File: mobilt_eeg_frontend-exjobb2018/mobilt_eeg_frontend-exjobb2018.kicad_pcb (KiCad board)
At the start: 2 copper layers, 95 x 90.5 mm, 126 parts, among them J1 Conn_02x04_Odd_Even, J11 Conn_01x02, J2 Conn_02x20_Odd_Even, J3 Conn_02x04_Odd_Even, J5 Data Header, J8 Conn_01x08, J9 Conn_01x04, P1 Conn_02x20_Odd_Even, SW1 SW_DIP_x01, SW2 SW_DIP_x01, U1 ADS1299-4PAG, U2 TPS60403DBVR, U3 TPS72325DBVT, U4 TPS73225DBVT, U5 TPS73233DBVT, U6 CAT24C256, U7 arduino_pro_mini_3V3_sparkfun, X1 X1G0044810050_SG7050CAN_2.048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

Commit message: savea for faen
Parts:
- moved J3 51.4 mm to (184.2, 229.6)
- moved J2 50.8 mm to (198.2, 229.6)
- moved R14 49.7 mm to (226.2, 218.2)
- moved R15 49.7 mm to (228.7, 218.2)
- moved R16 49.7 mm to (231.2, 218.2)
- moved R17 49.7 mm to (233.8, 218.2)
- moved R19 49.7 mm to (238.8, 218.2)
- moved R20 49.7 mm to (241.4, 218.2)
- moved R3 49.7 mm to (198.2, 218.2)
- moved R4 49.7 mm to (200.8, 218.2)
- moved R5 49.7 mm to (203.3, 218.2)
- moved R6 49.7 mm to (205.8, 218.2)
- moved R8 49.7 mm to (210.9, 218.2)
- moved R10 49.6 mm to (216.0, 218.2)
- moved R11 49.6 mm to (218.5, 218.2)
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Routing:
- net AGND: track 213.1 -> 156.2 mm, vias 25 -> 5
- net /SRB1: track 32.9 -> 0.00 mm
- net /SRB2: track 32.3 -> 0.00 mm
- net /IN8P: track 31.8 -> 0.00 mm
- net /IN7P: track 29.8 -> 0.00 mm
- net /IN8N: track 29.6 -> 0.00 mm
- net /IN1P: track 28.2 -> 0.00 mm
- net /IN7N: track 28.0 -> 0.00 mm
- net /IN6P: track 27.9 -> 0.00 mm
- net /IN2P: track 27.7 -> 0.00 mm
- net /IN5P: track 26.3 -> 0.00 mm
- net /IN3P: track 26.1 -> 0.00 mm
- net AVSS: track 145.2 -> 119.9 mm
- net /IN4P: track 25.3 -> 0.00 mm
- net /IN6N: track 25.2 -> 0.00 mm
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
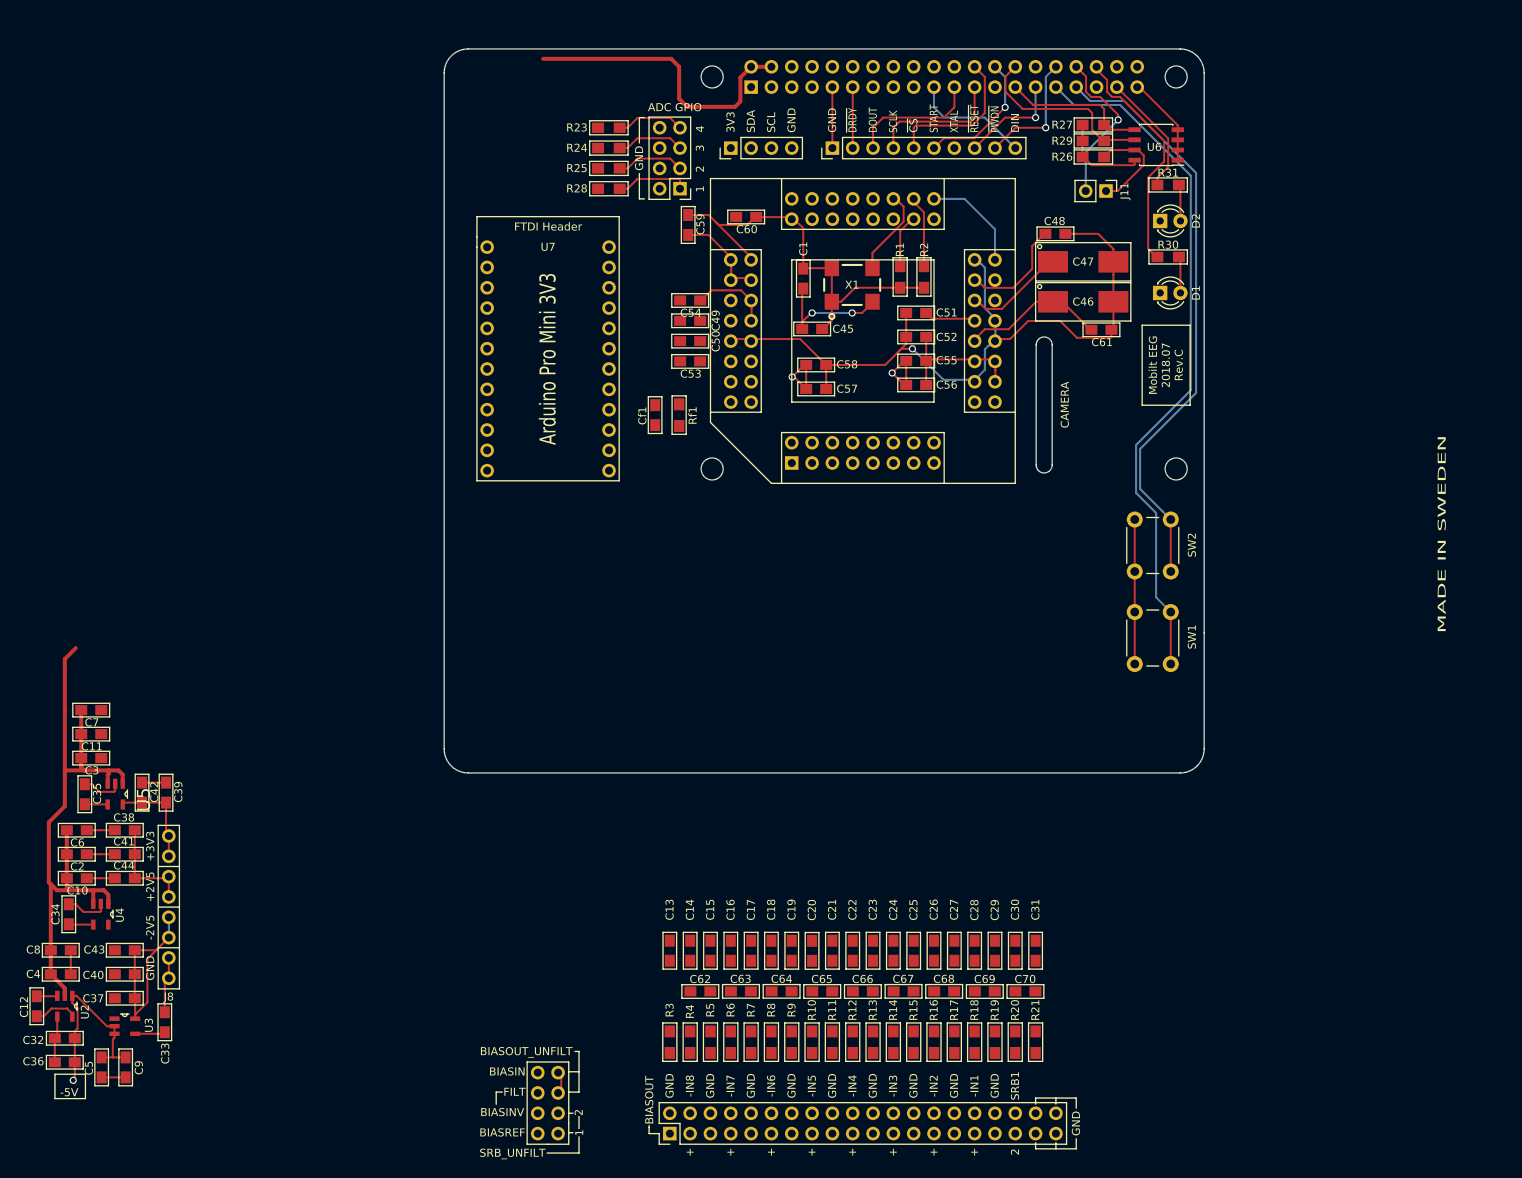
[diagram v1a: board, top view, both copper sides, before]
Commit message: Aligned most stuff except power supply.
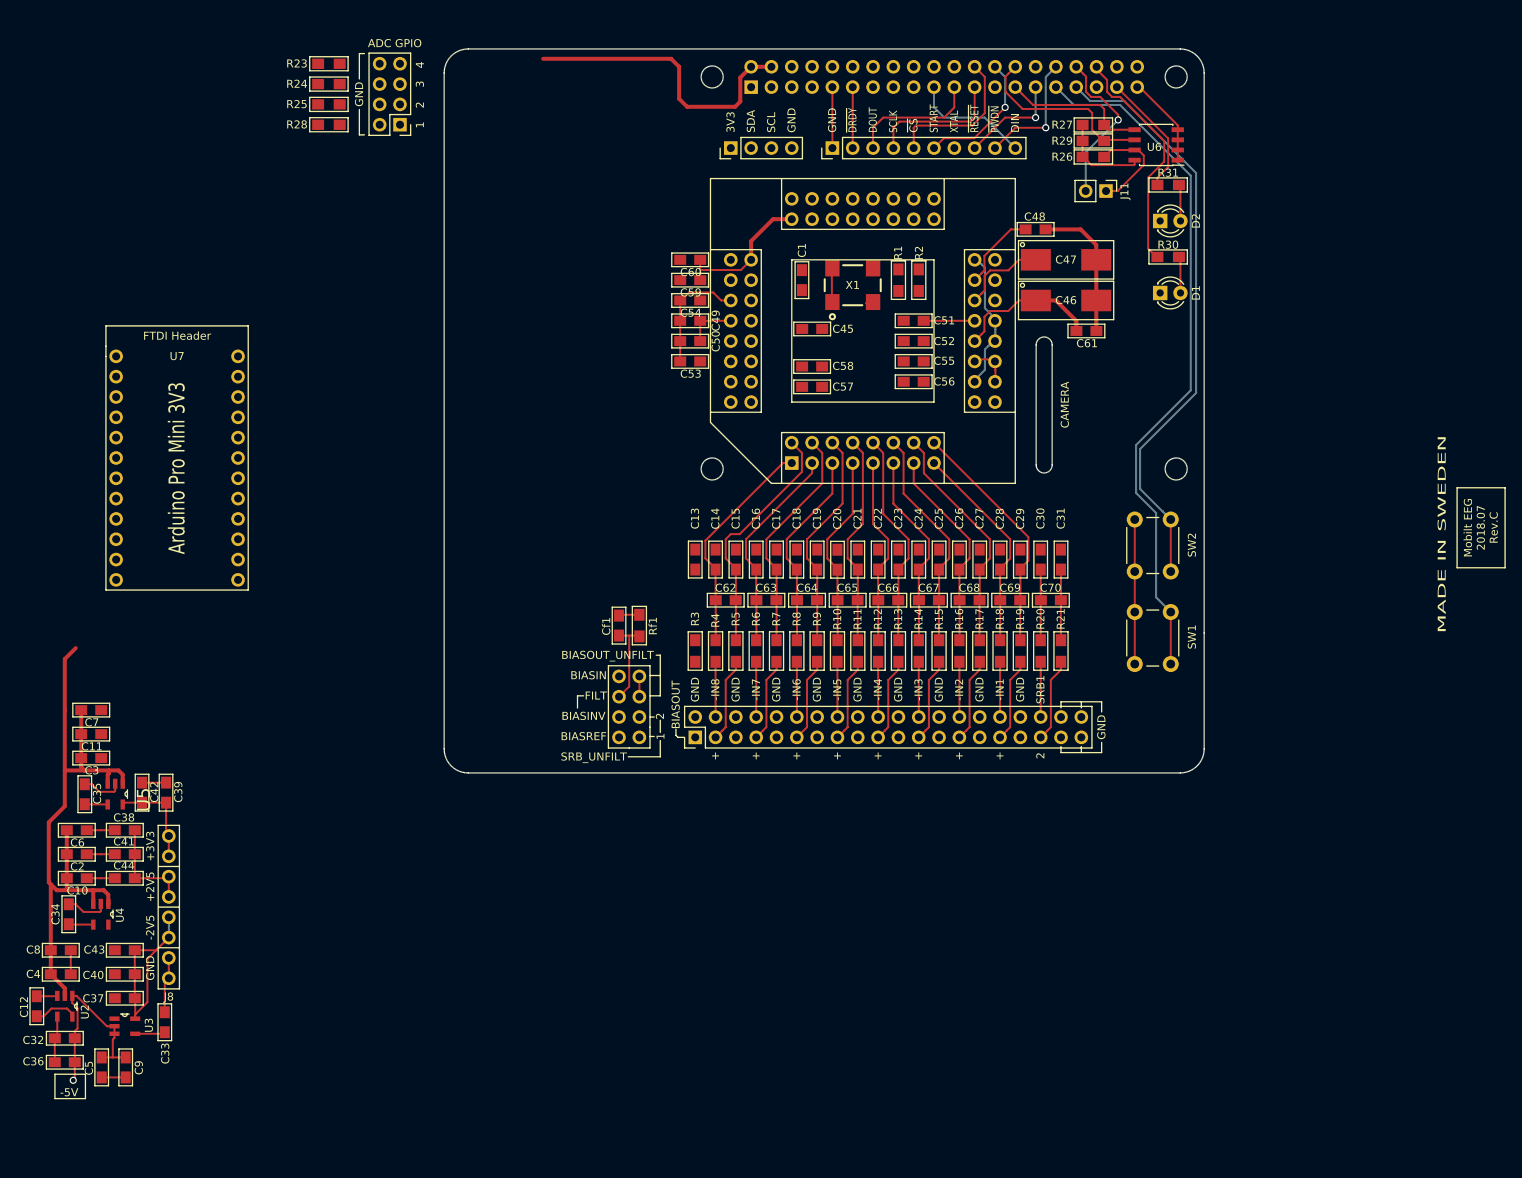
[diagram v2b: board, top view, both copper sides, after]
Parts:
- moved J3 50.6 mm to (194.4, 180.1)
- moved J2 49.6 mm to (201.4, 180.1)
- moved C62 49.0 mm to (205.2, 162.9)
- moved C65 49.0 mm to (220.4, 162.9)
- moved C66 49.0 mm to (225.5, 162.9)
- moved C69 49.0 mm to (240.8, 162.9)
- moved C70 49.0 mm to (245.8, 162.9)
- moved C13 49.0 mm to (201.4, 157.8)
- moved C14 49.0 mm to (203.9, 157.8)
- moved C15 49.0 mm to (206.5, 157.8)
- moved C16 49.0 mm to (209.0, 157.8)
- moved C17 49.0 mm to (211.5, 157.8)
- moved C18 49.0 mm to (214.1, 157.8)
- moved C19 49.0 mm to (216.6, 157.8)
- moved C20 49.0 mm to (219.2, 157.8)
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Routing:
- net AGND: track 156.2 -> 100.2 mm, vias 5 -> 1
- net AVSS: track 119.9 -> 75.8 mm, vias 1 -> 0
- net /IN8P: track 0.00 -> 30.3 mm
- net /IN1P: track 0.00 -> 30.0 mm
- net /IN2P: track 0.00 -> 29.2 mm
- net DVDD: track 75.0 -> 45.9 mm
- net /IN7P: track 0.00 -> 28.6 mm
- net /IN3P: track 0.00 -> 28.1 mm
- net /IN8N: track 0.00 -> 27.8 mm
- net /IN6P: track 0.00 -> 27.6 mm
- net /IN4P: track 0.00 -> 27.1 mm
- net /IN1N: track 0.00 -> 26.6 mm
- net /IN5P: track 0.00 -> 26.5 mm
- net /IN7N: track 0.00 -> 26.1 mm
- net /IN2N: track 0.00 -> 25.6 mm
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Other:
- board text added: "Electrode filtering 0.6350mm grid, origo pin1 raspi."
- board text added: "Notes All 2.54mm headers conform to 2.54mm grid with origo on Pi header pin 1. All SMD components conform to 1mm grid with origo on Pi header pin 1. Edge Cuts conform to 0.5mm grid with origo SNAPPED TO EXISTING LINES. ADC decoupling caps use 2.54mm grid"
- board text removed: "Notes All 2.54mm headers conform to 2.54mm grid with origo on Pi header pin 1. All SMD components conform to 1mm grid with origo on Pi header pin 1. Edge Cuts conform to 0.5mm grid with origo SNAPPED TO EXISTING LINES."

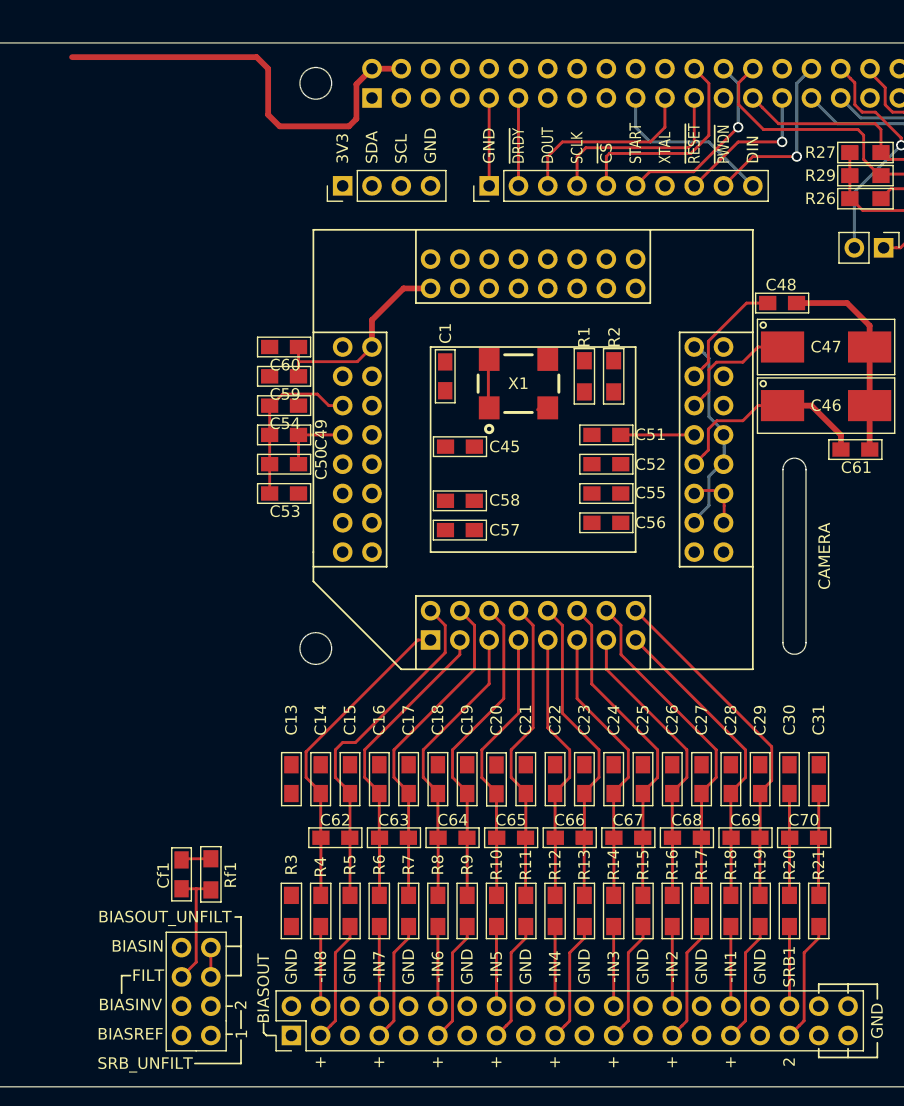
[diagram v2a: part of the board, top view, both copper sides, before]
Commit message: Added a few more traces and GND vias.
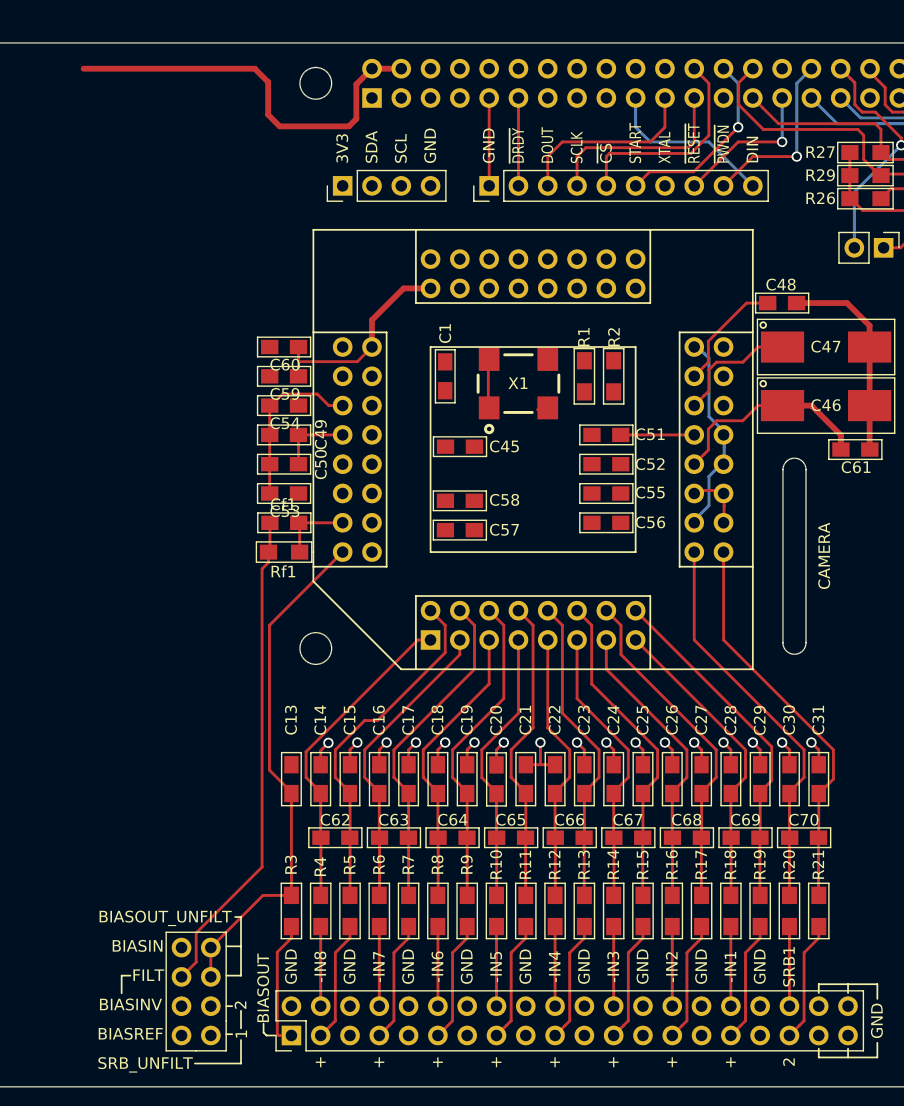
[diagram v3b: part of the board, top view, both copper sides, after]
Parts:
- moved Cf1 31.8 mm to (200.8, 135.6), turned to 180 degrees
- moved Rf1 28.7 mm to (200.8, 138.1), turned to 180 degrees
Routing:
- net /BIASOUT: track 2.54 -> 44.6 mm
- net AGND: track 100.2 -> 139.7 mm, vias 1 -> 18
- net Net-(Cf1-Pad2): track 10.7 -> 42.5 mm
- net /SRB1: track 8.85 -> 34.3 mm
- net /SRB2: track 8.85 -> 34.3 mm
- net /BIASOUT_FILTERED: track 0.00 -> 11.1 mm
- net /BIASINV: track 2.58 -> 6.38 mm
- net +5V: track 119.6 -> 117.5 mm
